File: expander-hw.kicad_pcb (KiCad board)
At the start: 2 copper layers, 80 x 50 mm, 28 parts, among them J1 Conn_ARM_JTAG_SWD_10, J2 USB_C_Receptacle_USB2.0_16P, J3 Conn_02x08_Odd_Even, U1 STM32U545RETxQ, U2 USBLC6-2SC6, U3 AZ1117-3.3, U4 SRDA3.3-4BTG, U5 SRDA3.3-4BTG, U6 SRDA3.3-4BTG

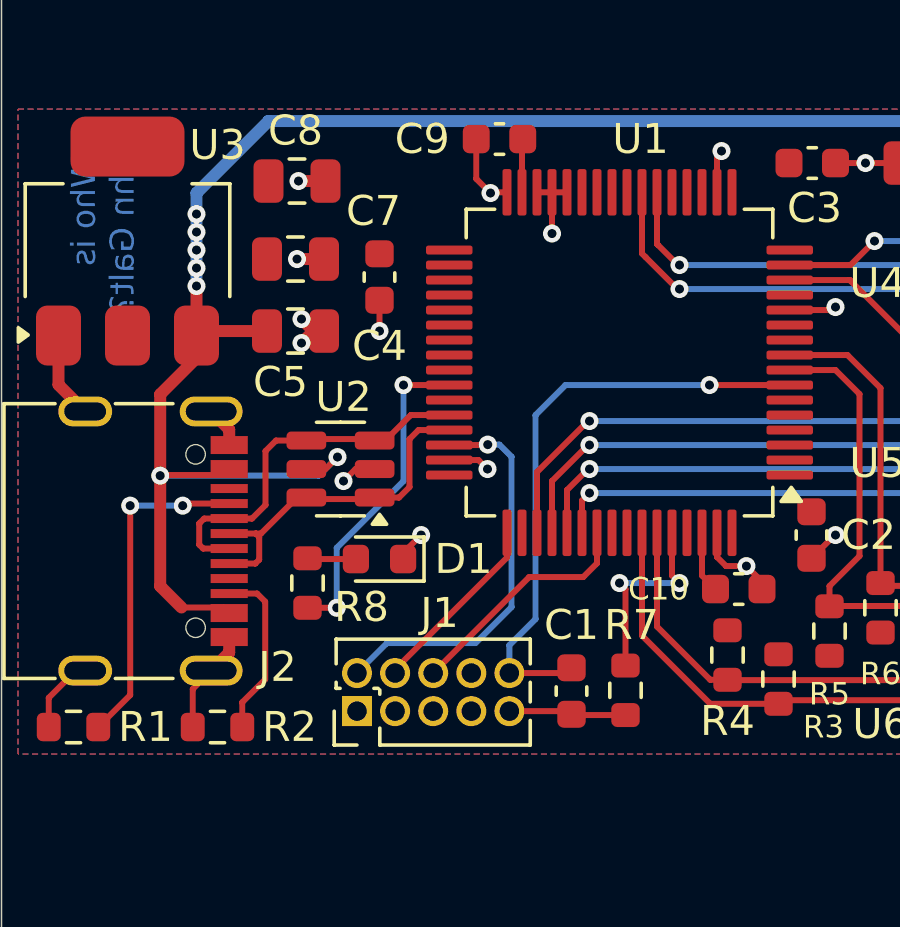
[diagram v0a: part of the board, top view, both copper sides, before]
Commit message: Add HW version + boot test point + SWD tag connector
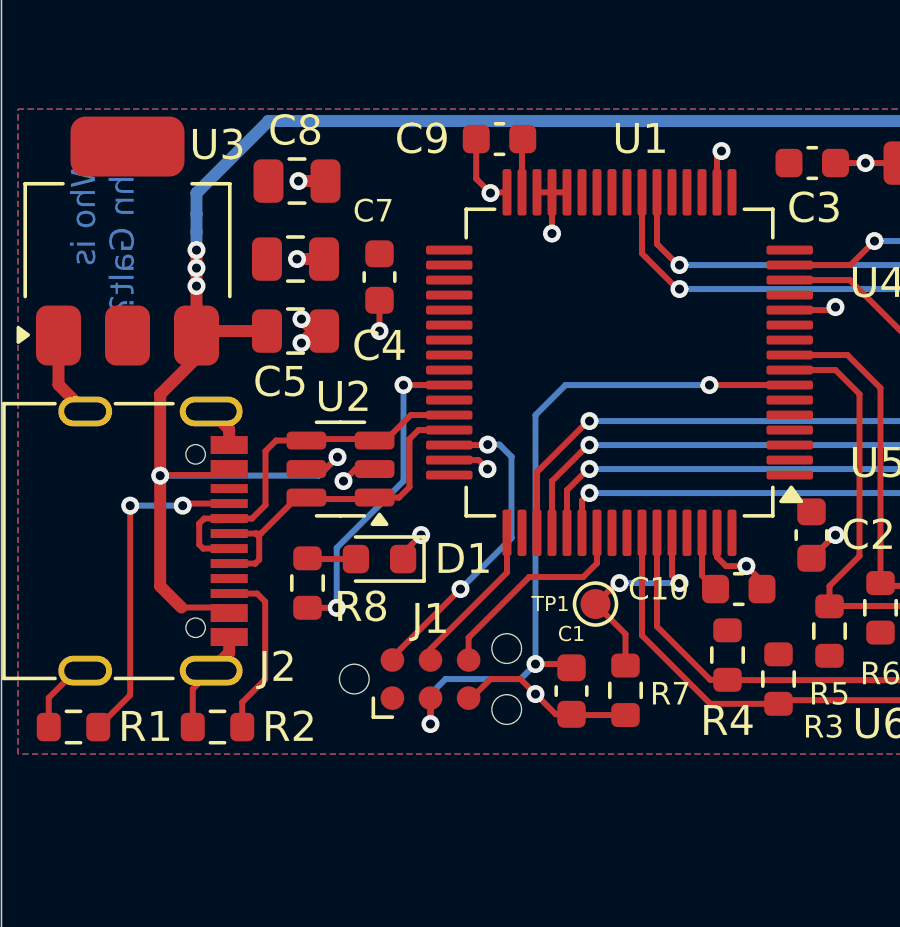
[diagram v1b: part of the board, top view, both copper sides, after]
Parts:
- added TP1: BOOT, TestPoint:TestPoint_Pad_D1.0mm, F.Cu at (128.0, 107.5)
- J1: value Conn_ARM_JTAG_SWD_10 -> Conn_ARM_SWD_TagConnect_TC2030-NL; footprint Connector_PinHeader_1.27mm:PinHeader_2x05_P1.27mm_Vertical -> Connector:Tag-Connect_TC2030-IDC-NL_2x03_P1.27mm_Vertical
- moved J1 2.67 mm to (122.5, 110.0), turned to 0 degrees
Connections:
- net Net-(U1-PH3) renamed /BOOT0
- J1 pad 3: GND -> /~{RESET}
- U1 pad 34: unconnected-(U1-PB13-Pad34) -> /HW_V0
- U1 pad 35: unconnected-(U1-PB14-Pad35) -> /HW_V1
- U1 pad 36: unconnected-(U1-PB15-Pad36) -> /HW_V2
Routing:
- net /~{RESET}: track 20.0 -> 24.5 mm, vias 1 -> 3
- net /SWDIO: track 13.3 -> 10.7 mm, vias 1 -> 2
- net GND: track 44.8 -> 47.0 mm, vias 21 -> 22
- net /SWDCLK: track 6.22 -> 5.30 mm
- net /SWO: track 7.99 -> 7.07 mm
- net /BOOT0: track 6.61 -> 7.33 mm
- net VBUS: vias 7 -> 5

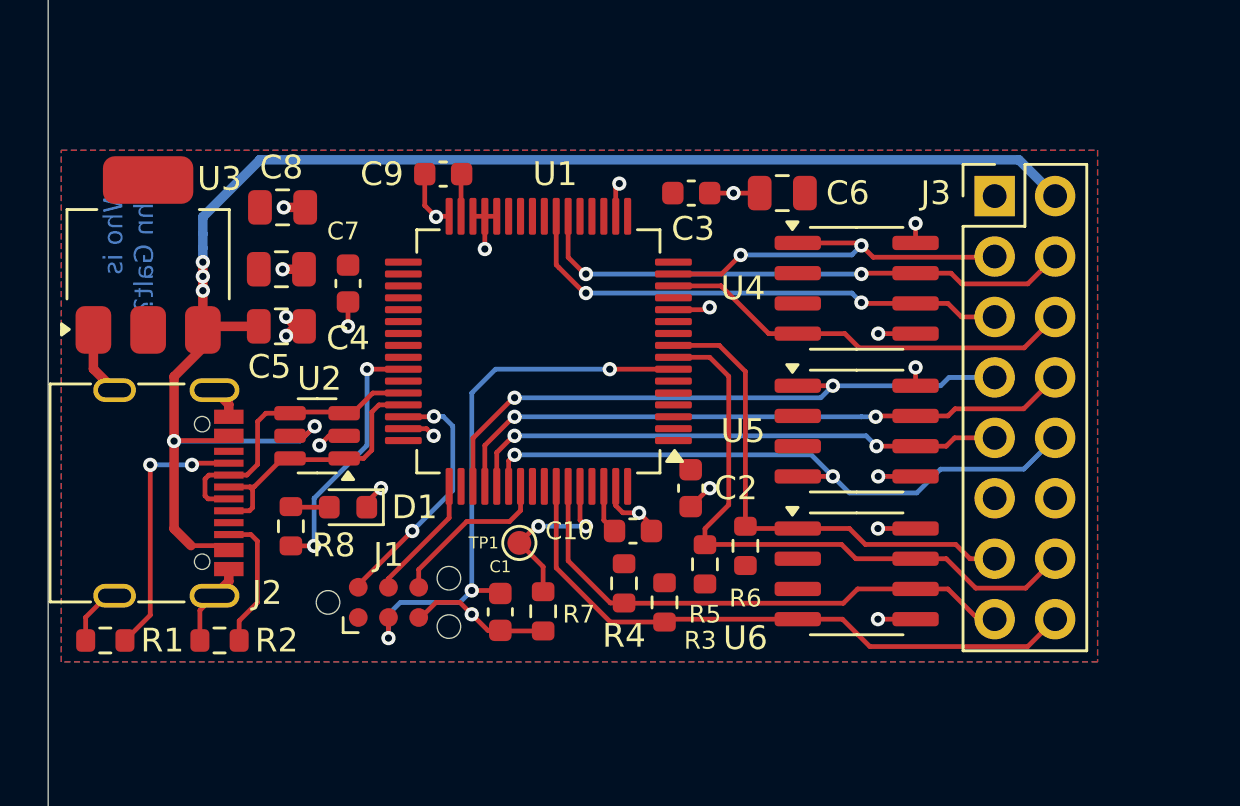
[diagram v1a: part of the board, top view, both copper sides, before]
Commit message: Switch to stm32h523 mcu
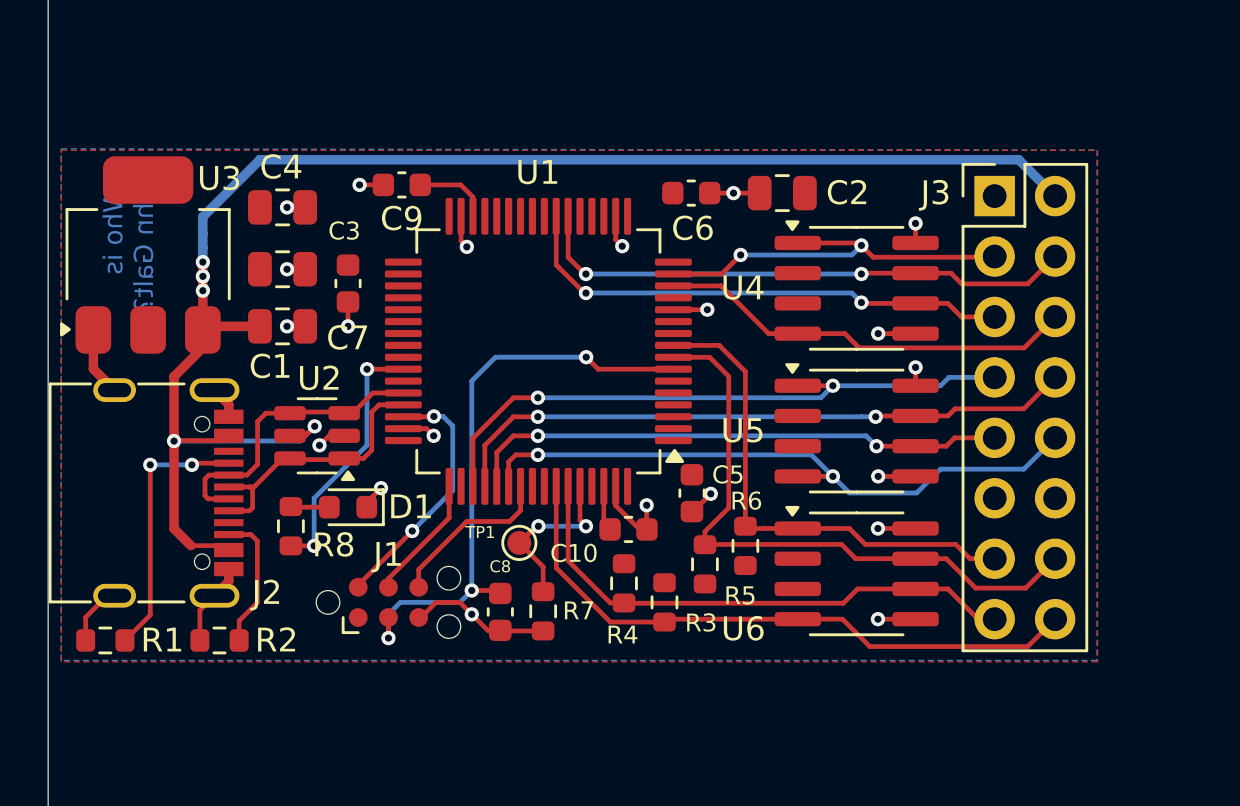
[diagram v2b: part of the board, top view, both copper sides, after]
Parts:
- C10, C9: value 100nF -> 2.2uF
- U1: value STM32U545RETxQ -> STM32H523RETx
- moved C9 1.80 mm to (123.1, 92.5), turned to 180 degrees
- moved C5 0.22 mm to (135.3, 105.4)
- moved C10 0.20 mm to (132.6, 106.9), turned to 0 degrees
- renumbered C5 to C1, C6 to C2, C7 to C3, C8 to C4, C2 to C5, C3 to C6, C4 to C7, C1 to C8
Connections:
- C10 pad 1: GND -> Net-(C10-Pad1)
- C10 pad 2: Net-(C10-Pad2) -> GND
- C9 pad 1: GND -> Net-(C9-Pad1)
- C9 pad 2: Net-(C9-Pad2) -> GND
- U1 pad 28: GND -> unconnected-(U1-PB2-Pad28)
- U1 pad 29: GND -> unconnected-(U1-PB10-Pad29)
- U1 pad 30: GND -> Net-(C9-Pad1)
- U1 pad 31: Net-(C9-Pad2) -> GND
- U1 pad 32: GND -> +3.3V
- U1 pad 33: +3.3V -> unconnected-(U1-PB12-Pad33)
- U1 pad 62: Net-(C10-Pad2) -> Net-(C10-Pad1)
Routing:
- net Net-(C9-Pad1): track 0.00 -> 3.36 mm
- net GND: track 47.0 -> 44.0 mm, vias 22 -> 21
- net Net-(C10-Pad2): track 2.06 -> 0.00 mm
- net Net-(C10-Pad1): track 0.00 -> 1.92 mm
- net Net-(C9-Pad2): track 1.79 -> 0.00 mm
- net /~{RESET}: track 24.5 -> 25.2 mm

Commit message: Save
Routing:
- net GND: track 44.0 -> 43.3 mm
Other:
- board text added: "HW-V1"
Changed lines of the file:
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@@
 		(tags "capacitor")
 		(property "Reference" "C5"
-			(at -0.762 -1.524 360)
+			(at -0.762 -1.524 0)
 			(layer "F.SilkS")
 			(effects
@@
 		(tags "LQFP QFP")
 		(property "Reference" "U1"
-			(at 0.022 7.502 360)
+			(at 0.022 7.502 0)
 			(layer "F.SilkS")
 			(effects
@@
 		)
 		(property "Value" "STM32H523RETx"
-			(at 0 7.4 360)
+			(at 0 7.4 0)
 			(layer "F.Fab")
 			(effects
@@
 		)
 		(fp_text user "${REFERENCE}"
-			(at 0 0 360)
+			(at 0 0 0)
 			(layer "F.Fab")
 			(effects
@@
 		(tags "capacitor")
 		(property "Reference" "C9"
-			(at 0 -1.43 360)
+			(at 0 -1.43 0)
 			(layer "F.SilkS")
 			(effects
@@
 		)
 		(property "Value" "2.2uF"
-			(at 0 1.43 360)
+			(at 0 1.43 0)
 			(layer "F.Fab")
 			(effects
@@
 		)
 		(fp_text user "${REFERENCE}"
-			(at 0 0 360)
+			(at 0 0 0)
 			(layer "F.Fab")
 			(effects
@@
 		)
 		(property "Value" "2.2uF"
-			(at 0 1.43 360)
+			(at 0 1.43 0)
 			(layer "F.Fab")
 			(effects
@@
 		)
 		(fp_text user "${REFERENCE}"
-			(at 0 0 360)
+			(at 0 0 0)
 			(layer "F.Fab")
 			(effects
@@
 		)
 	)
+	(gr_text "HW-V1"
+		(at 130.048 98.806 0)
+		(layer "B.SilkS")
+		(effects
+			(font
+				(size 1.5 1.5)
+				(thickness 0.3)
+				(bold yes)
+			)
+			(justify left bottom mirror)
+		)
+	)
 	(segment
 		(start 124.394202 102.2)
@@
 	)
 	(segment
-		(start 133.35 105.918)
-		(end 133.35 106.921)
-		(width 0.2)
-		(layer "F.Cu")
-		(net 2)
-	)
-	(segment
 		(start 125.7935 95.0595)
 		(end 125.55 94.816)
@@
 	)
 	(segment
-		(start 133.05159 106.934)
-		(end 132.05 105.93241)
-		(width 0.2)
-		(layer "F.Cu")
-		(net 2)
-	)
-	(segment
 		(start 126 110.5)
 		(end 126.675 111.175)
@@
 	)
 	(segment
+		(start 132.707384 106.394341)
+		(end 132.823341 106.394341)
+		(width 0.2)
+		(layer "F.Cu")
+		(net 2)
+	)
+	(segment
 		(start 125.55 94.816)
 		(end 125.55 93.775)
@@
 	)
 	(segment
+		(start 132.707384 106.394341)
+		(end 132.511931 106.394341)
+		(width 0.2)
+		(layer "F.Cu")
+		(net 2)
+	)
+	(segment
 		(start 110.68 109.72)
 		(end 110.99 109.72)
@@
 	)
 	(segment
-		(start 133.35 106.921)
-		(end 133.363 106.934)
-		(width 0.2)
-		(layer "F.Cu")
-		(net 2)
-	)
-	(segment
 		(start 114.575 111.6)
 		(end 114.575 110.335)
@@
 	)
 	(segment
+		(start 132.823341 106.394341)
+		(end 133.363 106.934)
+		(width 0.2)
+		(layer "F.Cu")
+		(net 2)
+	)
+	(segment
 		(start 132.323729 95.030534)
 		(end 132.05 94.756805)
@@
 	)
 	(segment
-		(start 133.363 106.934)
-		(end 133.05159 106.934)
+		(start 132.05 105.93241)
+		(end 132.05 105.125)
 		(width 0.2)
 		(layer "F.Cu")
@@
 	)
 	(segment
-		(start 135.999994 92.799994)
-		(end 136.999994 92.799994)
+		(start 133.363 106.934)
+		(end 133.05159 106.934)
 		(width 0.2)
 		(layer "F.Cu")
@@
 	)
 	(segment
-		(start 132.05 105.93241)
-		(end 132.05 105.125)
+		(start 135.999994 92.799994)
+		(end 136.999994 92.799994)
 		(width 0.2)
 		(layer "F.Cu")
@@
 		(net 2)
 	)
+	(segment
+		(start 132.511931 106.394341)
+		(end 132.05 105.93241)
+		(width 0.2)
+		(layer "F.Cu")
+		(net 2)
+	)
 	(via
 		(at 124.4 103)
@@
 	)
 	(via
-		(at 133.35 105.918)
+		(at 132.707384 106.394341)
 		(size 0.6)
 		(drill 0.3)
@@
 	)
 	(segment
-		(start 114.7 96.3)
-		(end 114.7 95.7)
-		(width 0.4)
-		(layer "F.Cu")
-		(net 13)
-	)
-	(segment
 		(start 114.7 99.3)
 		(end 113.49 100.51)
@@
 	)
 	(segment
-		(start 114.7 96.9)
-		(end 114.7 96.3)
-		(width 0.4)
-		(layer "F.Cu")
-		(net 13)
-	)
-	(segment
 		(start 113.49 100.51)
 		(end 113.49 103.22)
@@
 	)
 	(segment
+		(start 114.7 96.9)
+		(end 114.7 96.3)
+		(width 0.4)
+		(layer "B.Cu")
+		(net 13)
+	)
+	(segment
 		(start 114.7 95.1)
 		(end 114.7 94.5)
@@
 	)
 	(segment
+		(start 114.7 96.3)
+		(end 114.7 95.7)
+		(width 0.4)
+		(layer "B.Cu")
+		(net 13)
+	)
+	(segment
 		(start 114.7 95.7)
 		(end 114.7 95.1)
@@
 	)
 	(segment
-		(start 146.34 107.565006)
-		(end 146.94 108.165006)
+		(start 136.4 99.2)
+		(end 137.5 100.3)
 		(width 0.2)
 		(layer "F.Cu")
@@
 	)
 	(segment
-		(start 136.4 99.2)
-		(end 137.5 100.3)
+		(start 141.87 106.895006)
+		(end 142.54 107.565006)
 		(width 0.2)
 		(layer "F.Cu")
@@
 	)
 	(segment
-		(start 139.7 106.895006)
-		(end 141.87 106.895006)
+		(start 142.54 107.565006)
+		(end 146.34 107.565006)
 		(width 0.2)
 		(layer "F.Cu")
@@
 	)
 	(segment
-		(start 141.87 106.895006)
-		(end 142.54 107.565006)
+		(start 146.34 107.565006)
+		(end 146.94 108.165006)
 		(width 0.2)
 		(layer "F.Cu")
@@
 	)
 	(segment
-		(start 142.54 107.565006)
-		(end 146.34 107.565006)
+		(start 137.595006 106.895006)
+		(end 139.7 106.895006)
 		(width 0.2)
 		(layer "F.Cu")
@@
 	)
 	(segment
-		(start 137.595006 106.895006)
-		(end 139.7 106.895006)
+		(start 137.5 106.8)
+		(end 137.595006 106.895006)
 		(width 0.2)
 		(layer "F.Cu")
@@
 	)
 	(segment
-		(start 137.5 106.8)
-		(end 137.595006 106.895006)
+		(start 139.7 106.895006)
+		(end 141.87 106.895006)
 		(width 0.2)
 		(layer "F.Cu")

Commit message: Minor esthetical improvements
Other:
- board text added: "HW-V0"
- board text removed: "HW-V1"

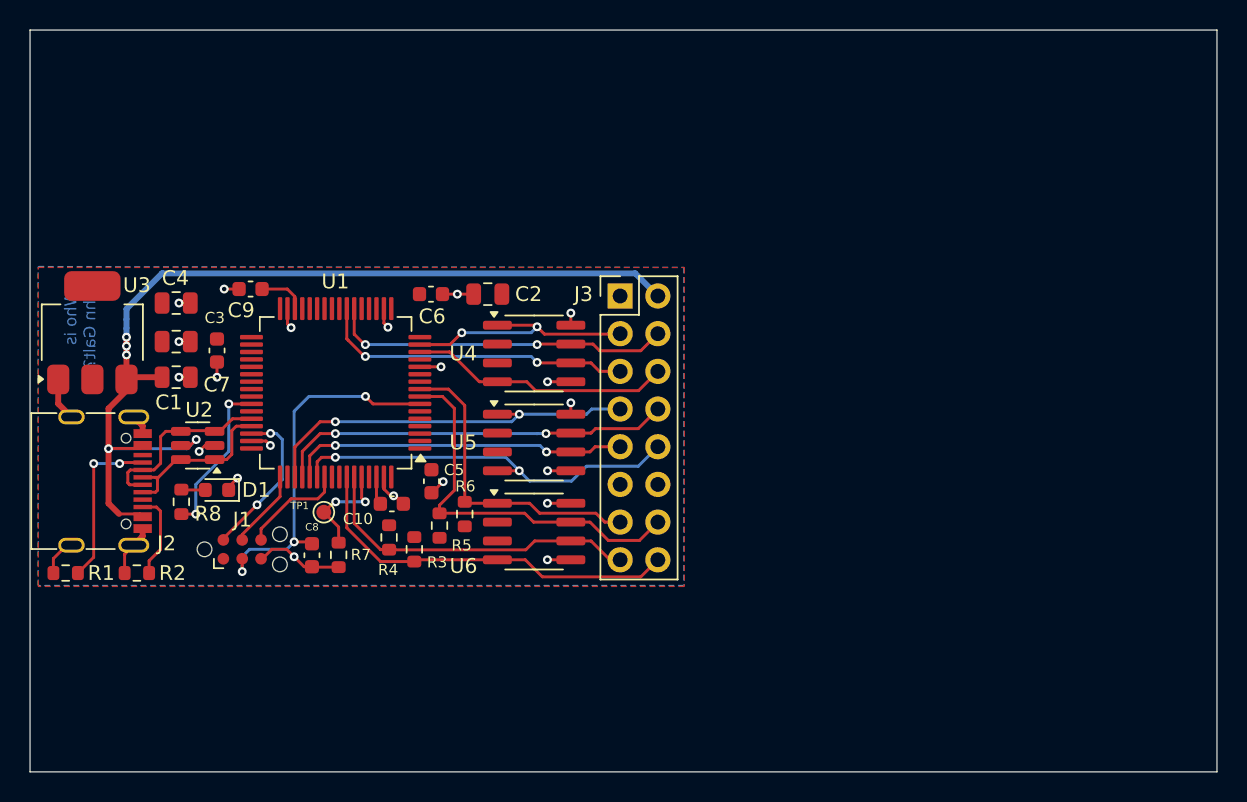
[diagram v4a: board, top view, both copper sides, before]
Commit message: Fix stm32h523 pinout
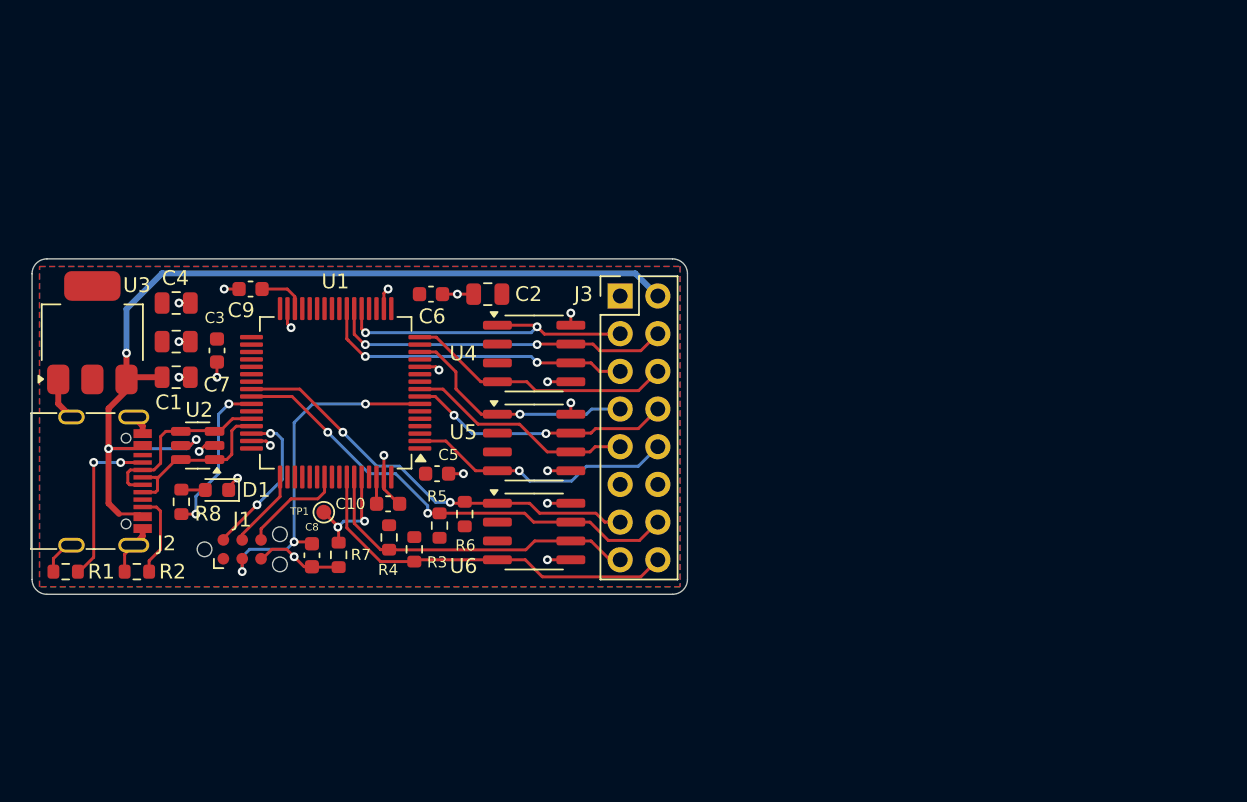
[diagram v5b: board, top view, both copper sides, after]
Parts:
- moved C5 0.63 mm to (135.6, 104.9), turned to 0 degrees
- moved C10 0.25 mm to (132.3, 106.9)
- moved R1 0.09 mm to (110.6, 111.5)
- moved R2 0.09 mm to (115.4, 111.5)
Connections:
- J3 pad 10: /SPI3_CS -> /SPI4_CS
- J3 pad 7: /SPI3_SCK -> /SPI4_SCK
- J3 pad 8: /SPI3_MISO -> /SPI4_MISO
- J3 pad 9: /SPI3_MOSI -> /SPI4_MOSI
- U1 pad 14: /SPI1_CS -> /SPI4_SCK
- U1 pad 15: /SPI1_SCK -> unconnected-(U1-PA1-Pad15)
- U1 pad 16: unconnected-(U1-PA2-Pad16) -> /SPI1_CS
- U1 pad 2: unconnected-(U1-PC13-Pad2) -> /SPI4_CS
- U1 pad 21: unconnected-(U1-PA5-Pad21) -> /SPI1_SCK
- U1 pad 33: unconnected-(U1-PB12-Pad33) -> /HW_V0
- U1 pad 34: /HW_V0 -> /HW_V1
- U1 pad 35: /HW_V1 -> /HW_V2
- U1 pad 36: /HW_V2 -> unconnected-(U1-PB15-Pad36)
- U1 pad 40: unconnected-(U1-PC9-Pad40) -> /I2C3_SDA
- U1 pad 41: unconnected-(U1-PA8-Pad41) -> /I2C3_SCL
- U1 pad 51: /SPI3_SCK -> unconnected-(U1-PC10-Pad51)
- U1 pad 52: /SPI3_MISO -> unconnected-(U1-PC11-Pad52)
- U1 pad 53: /SPI3_MOSI -> unconnected-(U1-PC12-Pad53)
- U1 pad 54: /SPI3_CS -> unconnected-(U1-PD2-Pad54)
- U1 pad 8: /I2C3_SCL -> /SPI4_MISO
- U1 pad 9: /I2C3_SDA -> /SPI4_MOSI
- U5 pad 1: /SPI3_SCK -> /SPI4_SCK
- U5 pad 4: /SPI3_CS -> /SPI4_CS
- U5 pad 6: /SPI3_MOSI -> /SPI4_MOSI
- U5 pad 7: /SPI3_MISO -> /SPI4_MISO
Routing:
- net /SPI3_CS: track 27.3 -> 0.00 mm, vias 2 -> 0
- net /SPI3_MISO: track 26.9 -> 0.00 mm, vias 2 -> 0
- net /SPI3_SCK: track 26.8 -> 0.00 mm, vias 2 -> 0
- net /SPI3_MOSI: track 23.0 -> 0.00 mm, vias 2 -> 0
- net /SPI4_CS: track 0.00 -> 18.2 mm, vias 0 -> 1
- net /SPI4_MISO: track 0.00 -> 17.8 mm, vias 0 -> 2
- net /SPI4_SCK: track 0.00 -> 16.4 mm, vias 0 -> 1
- net /SPI4_MOSI: track 0.00 -> 15.4 mm
- net /I2C3_SDA: track 21.0 -> 28.6 mm, vias 0 -> 2
- net /I2C3_SCL: track 26.1 -> 32.4 mm, vias 0 -> 2
- net /SPI1_SCK: track 16.9 -> 22.0 mm
- net /BOOT0: track 7.33 -> 8.88 mm
- net GND: track 43.3 -> 44.2 mm
- net /~{RESET}: track 25.2 -> 24.3 mm
- net VBUS: vias 5 -> 3
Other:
- board size 80 x 50 mm -> 44.2 x 22.6 mm
